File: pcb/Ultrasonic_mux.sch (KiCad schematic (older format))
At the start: 64 parts

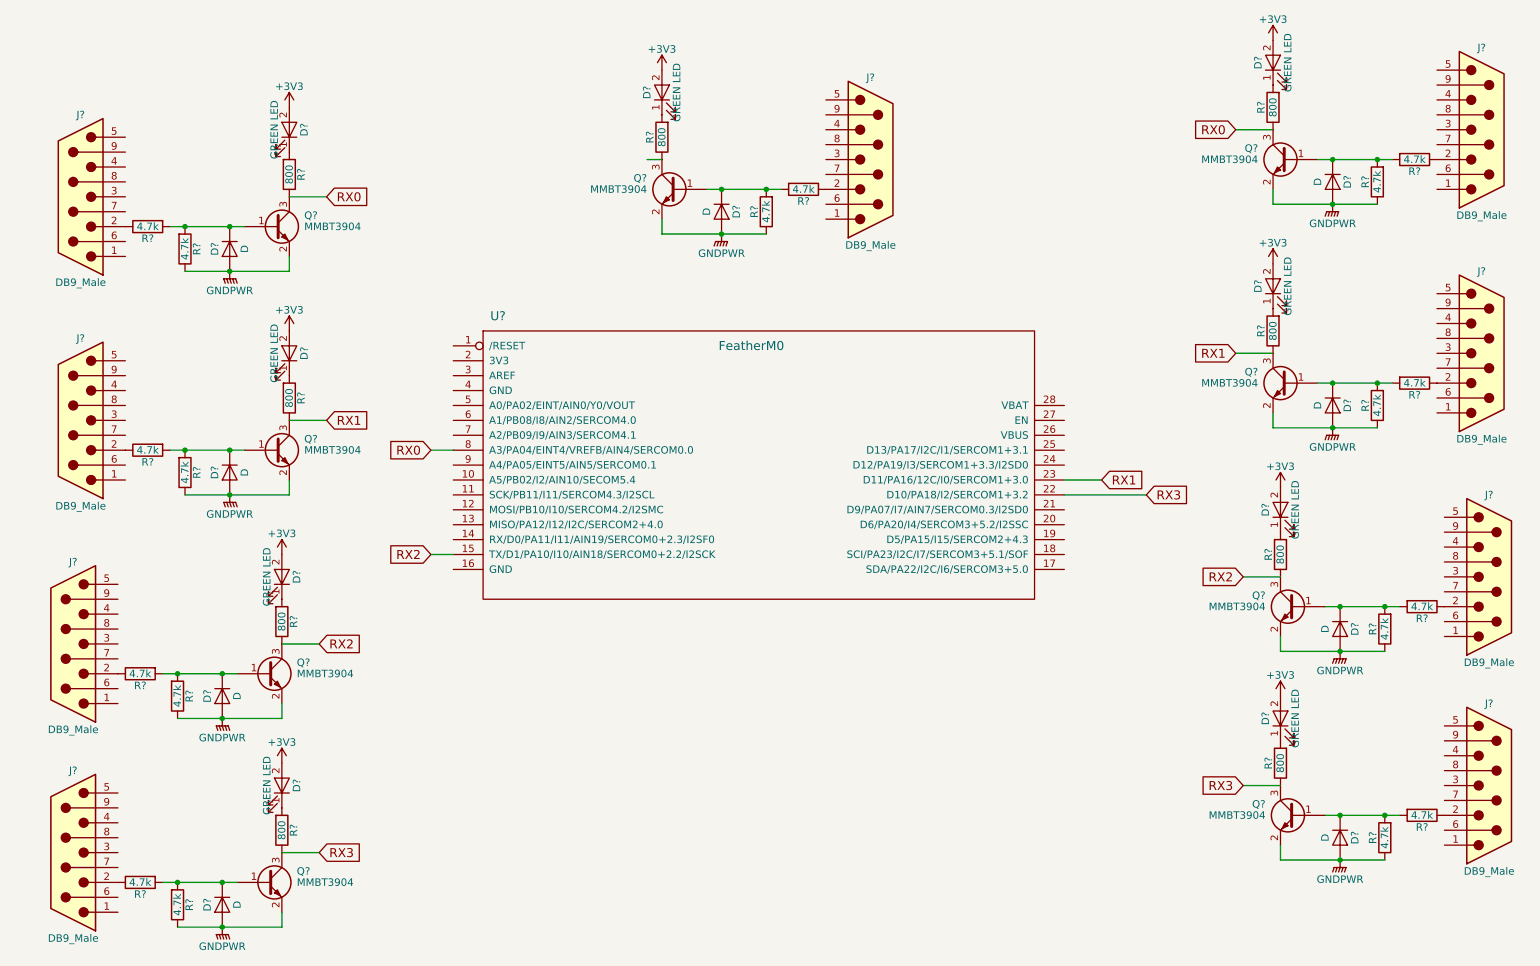
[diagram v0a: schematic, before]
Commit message: Finished RX ports and finished 3-pin connectors and power.
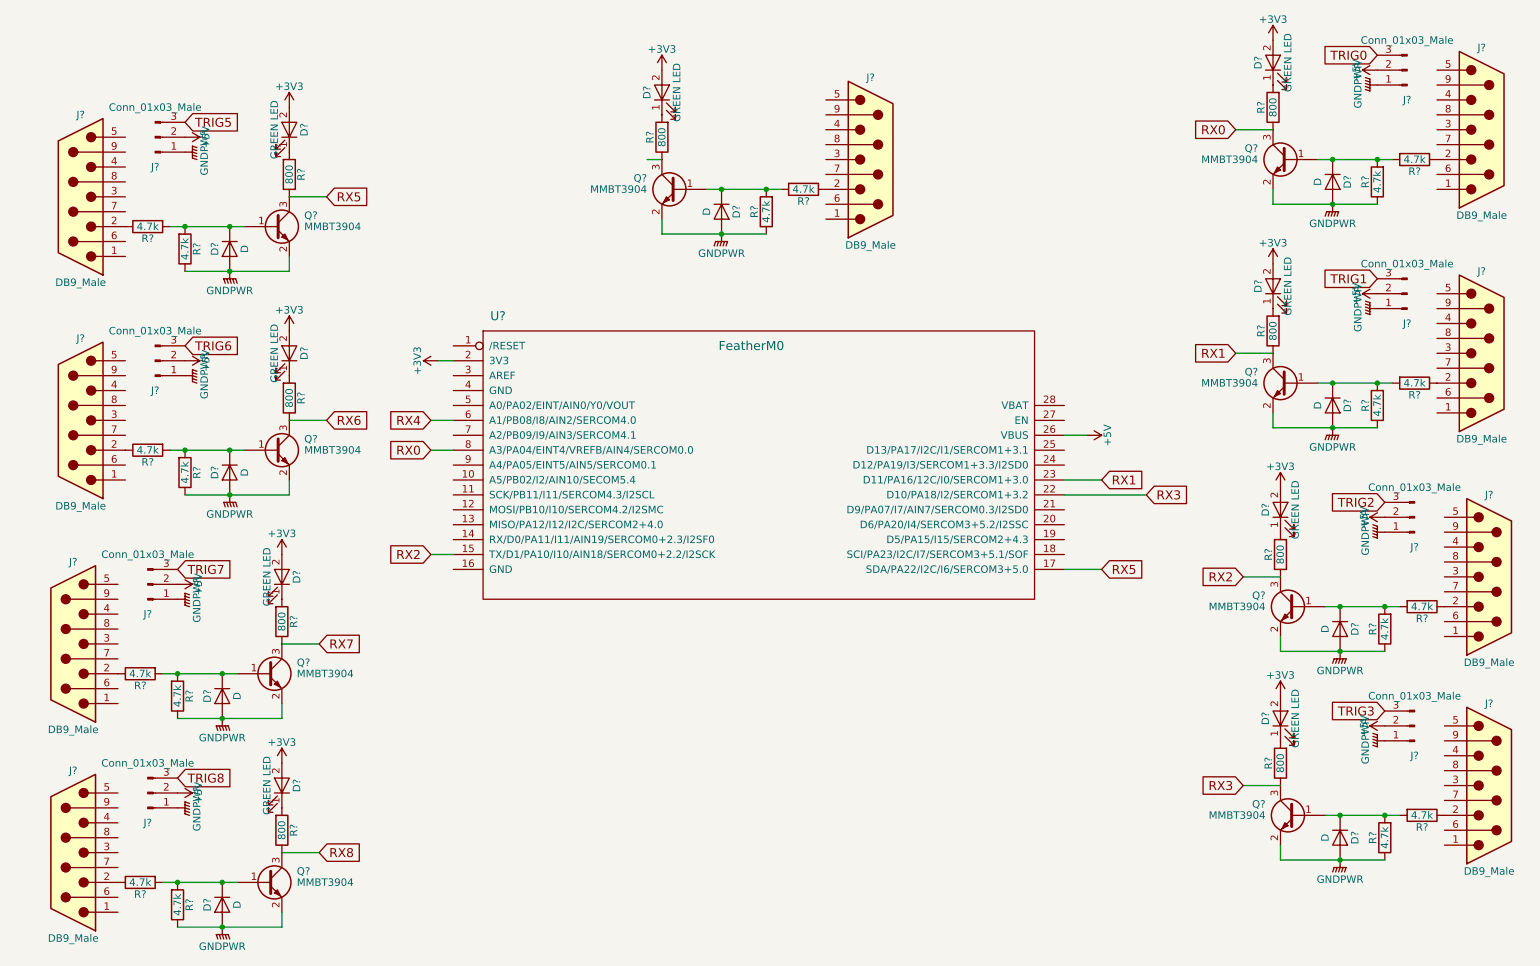
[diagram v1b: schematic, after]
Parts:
- added J? (x8): Conn_01x03_Male, symbol Conn_01x03_Male
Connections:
- net +3V3: now also U?.2 (3V3)
- net GNDPWR: now also J?.1 (Pin_1), J?.1 (Pin_1), J?.1 (Pin_1), J?.1 (Pin_1), J?.1 (Pin_1), J?.1 (Pin_1), J?.1 (Pin_1), J?.1 (Pin_1)
- net RX0: no longer Q?.3 (C), R?.1
- net RX1: no longer Q?.3 (C), R?.1
- net RX2: no longer Q?.3 (C), R?.1
- net RX3: no longer Q?.3 (C), R?.1
- net RX5: now reaches U?.17 (SDA/PA22/I2C/I6/SERCOM3+5.0)
- net RX5: now also Q?.3 (C), R?.1
- net +5V: now reaches U?.26 (VBUS)
- net +5V: now also J?.2 (Pin_2), J?.2 (Pin_2), J?.2 (Pin_2), J?.2 (Pin_2), J?.2 (Pin_2), J?.2 (Pin_2), J?.2 (Pin_2), J?.2 (Pin_2)
- net RX4: now reaches U?.6 (A1/PB08/I8/AIN2/SERCOM4.0)
- new net RX6: Q?.3 (C), R?.1
- new net RX7: Q?.3 (C), R?.1
- new net RX8: Q?.3 (C), R?.1
- new net TRIG0: J?.3 (Pin_3)
- new net TRIG1: J?.3 (Pin_3)
- new net TRIG2: J?.3 (Pin_3)
- new net TRIG3: J?.3 (Pin_3)
- new net TRIG5: J?.3 (Pin_3)
- new net TRIG6: J?.3 (Pin_3)
- new net TRIG7: J?.3 (Pin_3)
- new net TRIG8: J?.3 (Pin_3)

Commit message: Getting rid of ports 7 and 8, starting to label indicators/triggers.
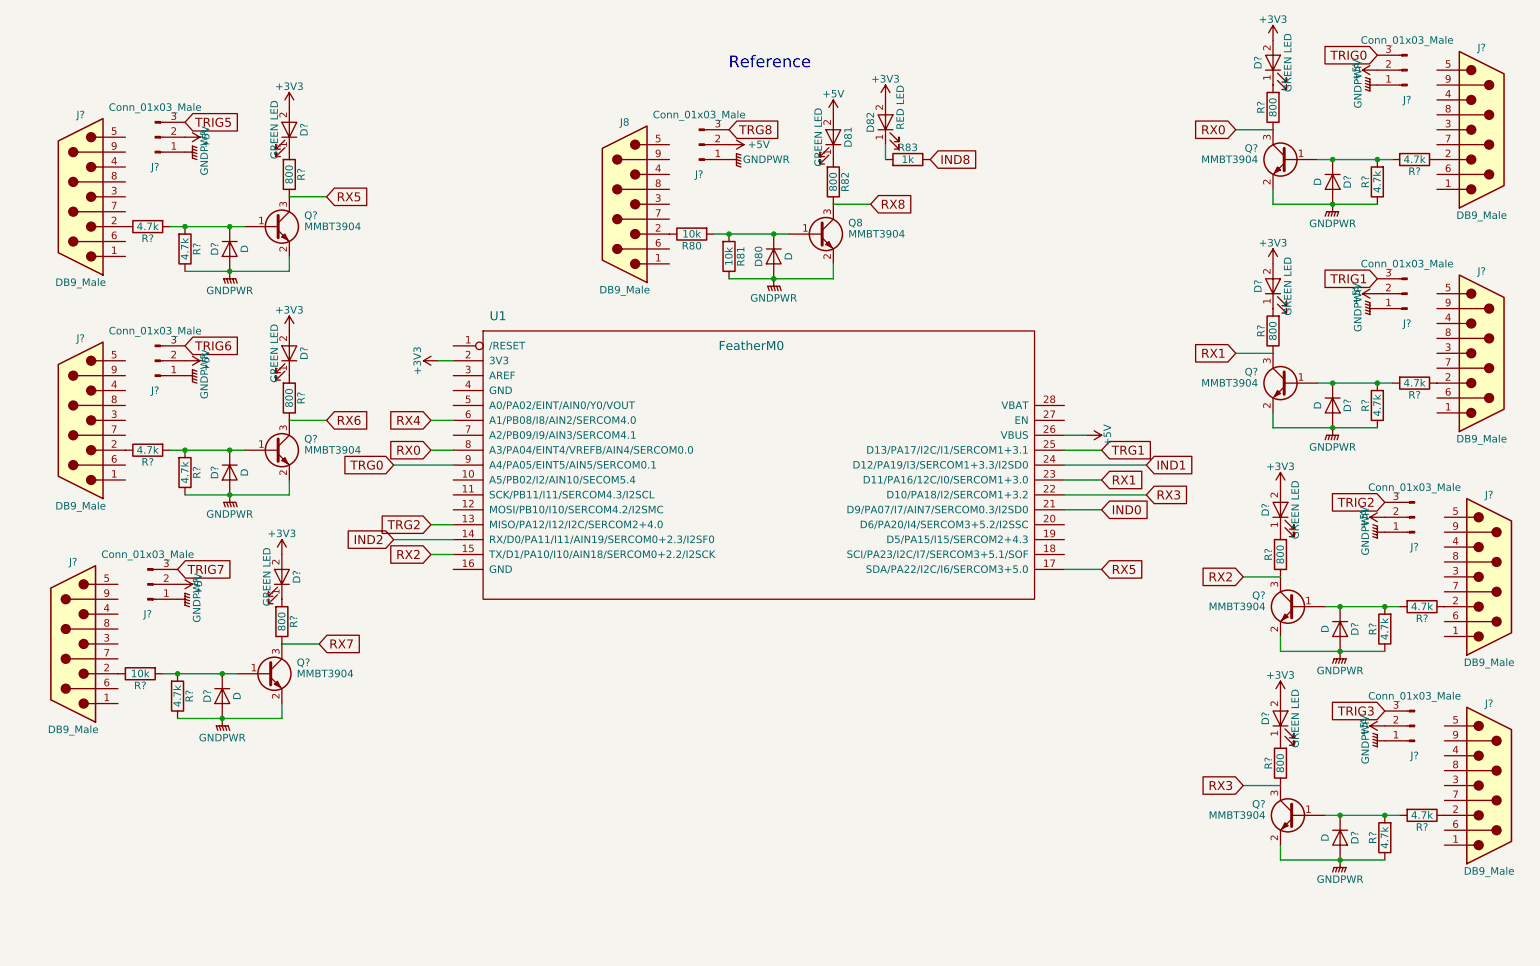
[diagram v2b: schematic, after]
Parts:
- removed D?: D, symbol D
- removed D?: GREEN LED, symbol LED
- removed J?: DB9_Male, symbol DB9_Male
- removed Q?: MMBT3904, TO_SOT_Packages_SMD:SOT-23, symbol MMBT3904
- removed R? (x2): 4.7k, symbol R
- removed R?: 800, symbol R
- added D82: RED LED, symbol LED
- added R83: 1k, symbol R
- R80, R81: renamed from R?; value 4.7k -> 10k
- R?: value 4.7k -> 10k
- gave numbers to parts that had none: 6
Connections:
- net +3V3: now also D82.2 (A); no longer D81.2 (A)
- net +5V: now also D81.2 (A)
- net TRG2: now reaches U1.13 (MISO/PA12/I12/I2C/SERCOM2+4.0)
- net IND2: now reaches U1.14 (RX/D0/PA11/I11/AIN19/SERCOM0+2.3/I2SF0)
- net IND0: now reaches U1.21 (D9/PA07/I7/AIN7/SERCOM0.3/I2SD0)
- net IND1: now reaches U1.24 (D12/PA19/I3/SERCOM1+3.3/I2SD0)
- net TRG1: now reaches U1.25 (D13/PA17/I2C/I1/SERCOM1+3.1)
- net TRG0: now reaches U1.9 (A4/PA05/EINT5/AIN5/SERCOM0.1)
- net TRIG8 renamed TRG8
- new net: D82.1 (K), R83.2
- new net IND8: R83.1
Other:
- note added: "Reference"
- moved on the sheet: D80, D81, J8, J?, Q8, R80, R81, R82

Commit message: Finished labeling indicators/triggers and organized layout.
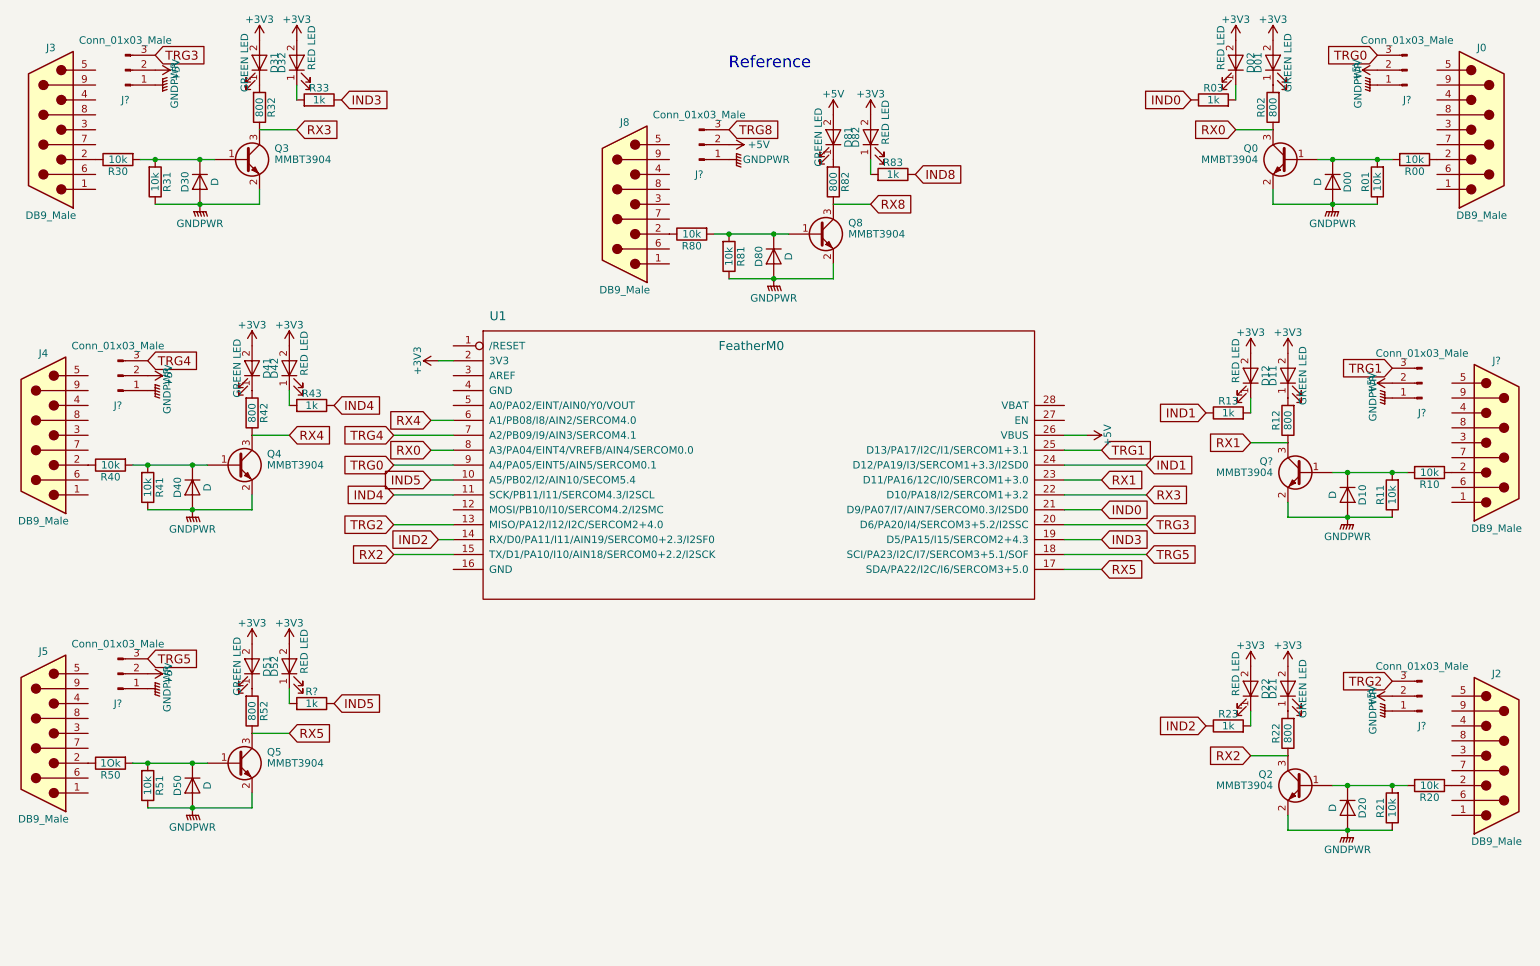
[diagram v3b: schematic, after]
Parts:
- removed D?: D, symbol D
- removed D?: GREEN LED, symbol LED
- removed J?: DB9_Male, symbol DB9_Male
- removed J?: Conn_01x03_Male, symbol Conn_01x03_Male
- removed Q?: MMBT3904, TO_SOT_Packages_SMD:SOT-23, symbol MMBT3904
- removed R?: 4.7k, symbol R
- removed R?: 10k, symbol R
- removed R?: 800, symbol R
- added D02, D12, D22, D32, D42, D52: RED LED, symbol LED
- added R03, R13, R23, R33, R43, R?: 1k, symbol R
- R00, R01, R10, R11, R20, R21, R30, R31, R40, R41, R51: renamed from R?; value 4.7k -> 10k
- R50: renamed from R?; value 4.7k -> 1Ok
- gave numbers to parts that had none: 28
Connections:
- net RX6 is gone; now on net RX5: Q5.3 (C), R52.1
- net TRIG0 is gone; now on net TRG0: J?.3 (Pin_3)
- net TRIG1 is gone; now on net TRG1: J?.3 (Pin_3)
- net TRIG2 is gone; now on net TRG2: J?.3 (Pin_3)
- net TRIG3 is gone; now on net TRG3: J?.3 (Pin_3)
- net TRIG5 is gone; now on net TRG4: J?.3 (Pin_3)
- net TRIG6 is gone; now on net TRG5: J?.3 (Pin_3)
- net +3V3: now also D02.2 (A), D12.2 (A), D22.2 (A), D32.2 (A), D42.2 (A), D52.2 (A)
- net IND0: now also R03.1
- net IND1: now also R13.1
- net IND2: now also R23.1
- net RX4: now also Q4.3 (C), R42.1
- net RX5: no longer Q4.3 (C), R42.1
- net IND5: now reaches U1.10 (A5/PB02/I2/AIN10/SECOM5.4)
- net IND5: now also R?.1
- net IND4: now reaches U1.11 (SCK/PB11/I11/SERCOM4.3/I2SCL)
- net IND4: now also R43.1
- net TRG5: now reaches U1.18 (SCI/PA23/I2C/I7/SERCOM3+5.1/SOF)
- net IND3: now reaches U1.19 (D5/PA15/I15/SERCOM2+4.3)
- net IND3: now also R33.1
- net TRG3: now reaches U1.20 (D6/PA20/I4/SERCOM3+5.2/I2SSC)
- net TRG4: now reaches U1.7 (A2/PB09/I9/AIN3/SERCOM4.1)
- new net: D12.1 (K), R13.2
- new net: D02.1 (K), R03.2
- new net: D22.1 (K), R23.2
- new net: D32.1 (K), R33.2
- new net: D42.1 (K), R43.2
- new net: D52.1 (K), R?.2
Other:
- moved on the sheet: D10, D11, D20, D21, D30, D31, D40, D41, D50, D51, D82, J2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

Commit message: References
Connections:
- net GNDPWR: now also J8.5
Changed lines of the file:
@@
 F 3 "" H 5550 1500 50  0001 C CNN
 	1    5550 1550
-	0    -1   -1   0
+	1    0    0    -1
 $EndComp
 $Comp
@@
 Wire Wire Line
 	3550 3700 3700 3700
+$Comp
+L GNDPWR #PWR?
+U 1 1 5A73B5E5
+P 5250 1450
+F 0 "#PWR?" H 5250 1250 50  0001 C CNN
+F 1 "GNDPWR" H 5250 1320 50  0000 C CNN
+F 2 "" H 5250 1400 50  0001 C CNN
+F 3 "" H 5250 1400 50  0001 C CNN
+	1    5250 1450
+	1    0    0    -1
+$EndComp
+Wire Notes Line
+	5500 900  5250 900
+Wire Notes Line
+	5250 900  5250 1500
+Wire Notes Line
+	6150 900  6300 900
+Wire Notes Line
+	6300 900  6300 1050
+Wire Notes Line
+	5550 1000 5550 1550
+Wire Wire Line
+	5150 1450 5250 1450
 $EndSCHEMATC
